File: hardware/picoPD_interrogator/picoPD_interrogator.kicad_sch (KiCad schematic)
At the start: 34 parts, among them Q1 rohm-RE1C002UN, Q2 rohm-RE1C002UN, Q3 rohm-RE1C002UN, Q4 rohm-RE1C002UN, U2 ST-LM393QT

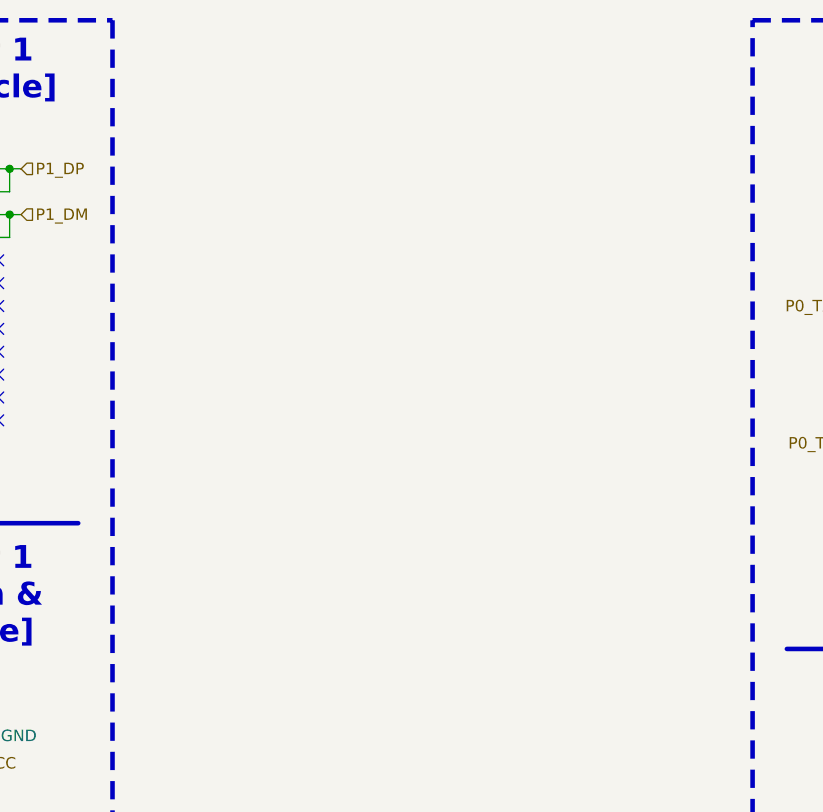
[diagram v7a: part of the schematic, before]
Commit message: Schematic: Working on TI voltage regulator.
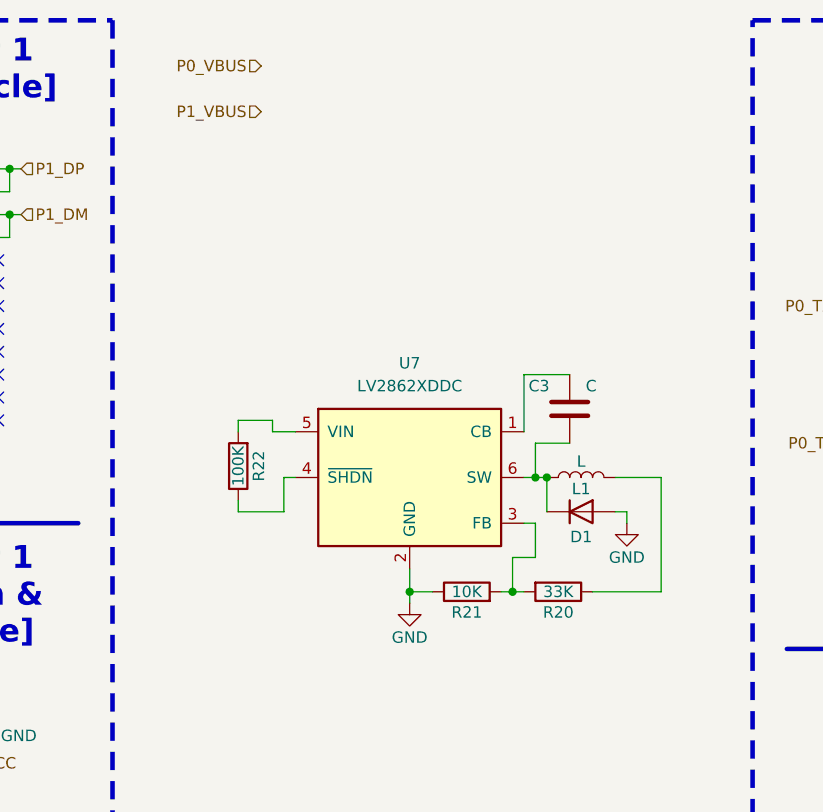
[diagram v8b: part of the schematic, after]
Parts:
- added C3: C, symbol Device:C
- added D1: D, symbol Device:D
- added L1: L, symbol Device:L
- added R20: 33K, symbol Device:R
- added R21: 10K, symbol Device:R
- added R22: 100K, symbol Device:R
- added U7: LV2862XDDC, Package_TO_SOT_SMD:SOT-23-6, symbol Regulator_Switching:LV2862XDDC
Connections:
- net GND: now also D1.2 (A), R21.1, U7.2 (GND)
- new net: C3.1, U7.1 (CB)
- new net: R20.2, R21.2, U7.3 (FB)
- new net: R22.1, U7.4 (~{SHDN})
- new net: R22.2, U7.5 (VIN)
- new net: C3.2, D1.1 (K), L1.1, U7.6 (SW)
- new net: L1.2, R20.1
